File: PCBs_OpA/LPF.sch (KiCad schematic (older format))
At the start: 9 parts, among them J2 ANT

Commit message: operational amplifier Direct detection receiver
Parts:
- L10, L6, L8: footprint Choke_Axial_ThroughHole:Choke_Horizontal_RM20mm -> Choke_Toroid_ThroughHole:Choke_Toroid_6,5x13mm_Vertical
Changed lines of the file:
@@
 F 0 "L6" V 5400 2450 50  0000 L CNN
 F 1 "1.32uH" V 5300 2250 50  0000 L CNN
-F 2 "Choke_Axial_ThroughHole:Choke_Horizontal_RM20mm" H 5200 2400 50  0001 C CNN
+F 2 "Choke_Toroid_ThroughHole:Choke_Toroid_6,5x13mm_Vertical" H 5200 2400 50  0001 C CNN
 F 3 "" H 5200 2400 50  0001 C CNN
 	1    5200 2400
@@
 F 0 "L8" V 6050 2450 50  0000 L CNN
 F 1 "1.72uH" V 5950 2250 50  0000 L CNN
-F 2 "Choke_Axial_ThroughHole:Choke_Horizontal_RM20mm" H 5850 2400 50  0001 C CNN
+F 2 "Choke_Toroid_ThroughHole:Choke_Toroid_6,5x13mm_Vertical" H 5850 2400 50  0001 C CNN
 F 3 "" H 5850 2400 50  0001 C CNN
 	1    5850 2400
@@
 F 0 "L10" V 6700 2450 50  0000 L CNN
 F 1 "1.32uH" V 6600 2250 50  0000 L CNN
-F 2 "Choke_Axial_ThroughHole:Choke_Horizontal_RM20mm" H 6500 2400 50  0001 C CNN
+F 2 "Choke_Toroid_ThroughHole:Choke_Toroid_6,5x13mm_Vertical" H 6500 2400 50  0001 C CNN
 F 3 "" H 6500 2400 50  0001 C CNN
 	1    6500 2400

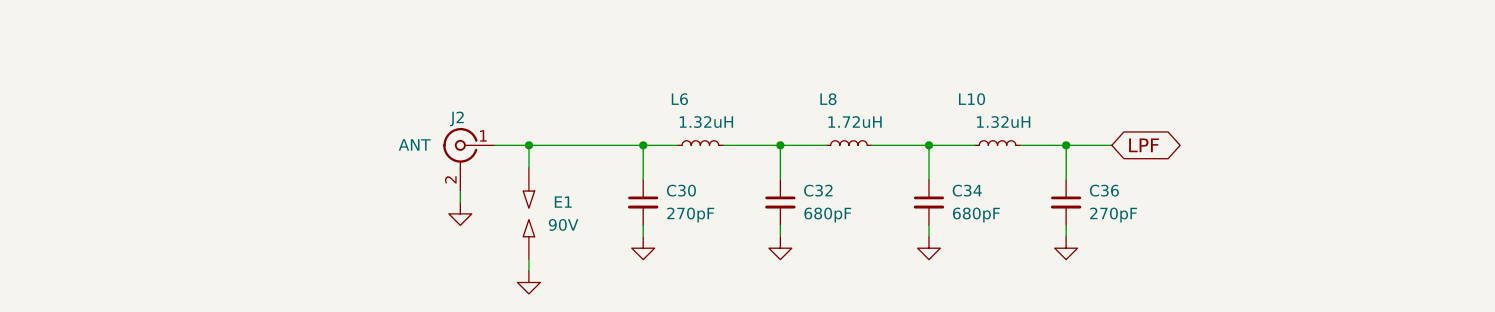
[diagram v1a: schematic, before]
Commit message: add LPF/HPF RFSimm models
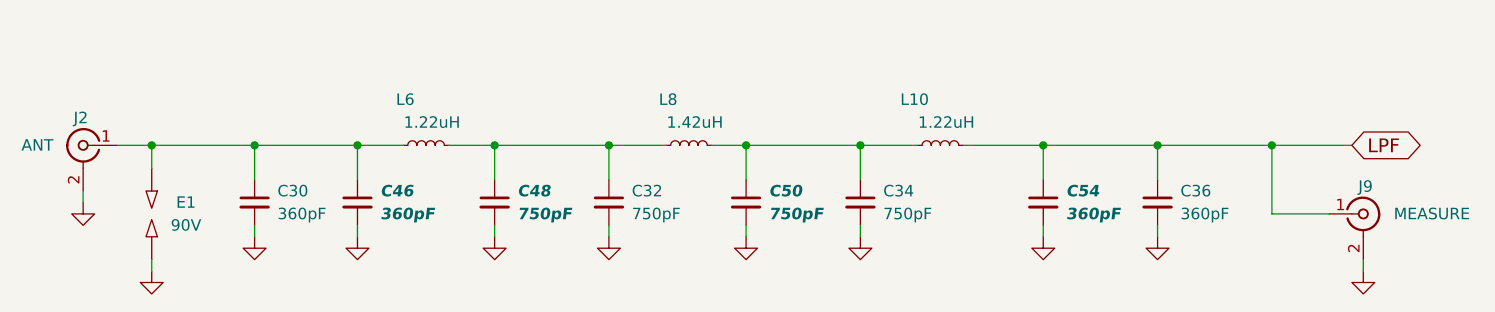
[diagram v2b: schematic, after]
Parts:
- added C46, C54: 360pF, LCSDR:C_1206_0603, symbol C_Small
- added C48, C50: 750pF, LCSDR:C_1206_0603, symbol C_Small
- added J9: MEASURE, LCSDR:U.FL_Molex_MCRF_73412-0110_Vertical, symbol Conn_Coaxial
- C30, C36: value 270pF -> 360pF
- C32, C34: value 680pF -> 750pF
- L10, L6: value 1.32uH -> 1.22uH
- L8: value 1.72uH -> 1.42uH
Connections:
- net GND: now also C46.2, C48.2, C50.2, C54.2, J9.2 (Ext)
- net LPF: now also C54.1, J9.1 (In)
- net at C30.1, E1.1, J2.1 (In)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: now also C46.1
- net at C32.1, L6.2, L8.1: now also C48.1
- net at C34.1, L10.1, L8.2: now also C50.1
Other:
- moved on the sheet: C30, C32, C34, C36, E1, J2, L10, L6, L8

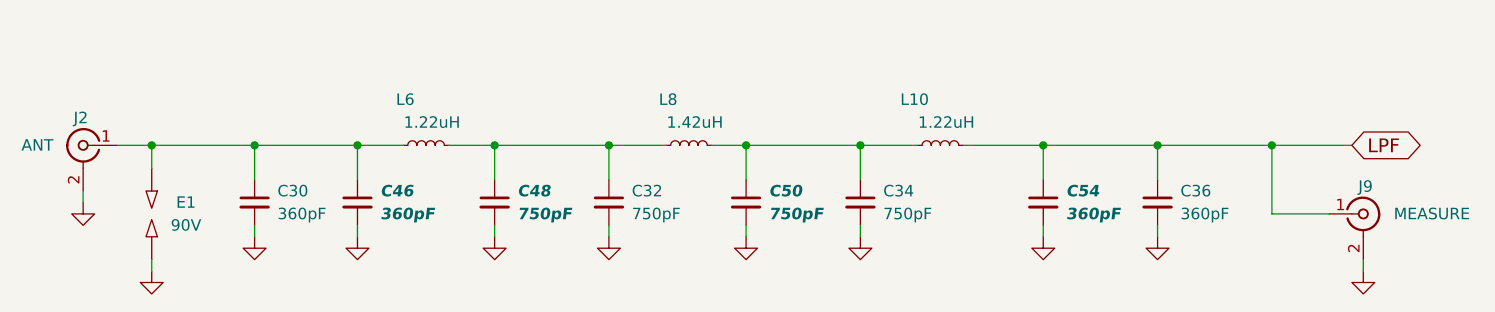
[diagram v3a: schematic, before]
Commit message: add text to HPF/LPF sch
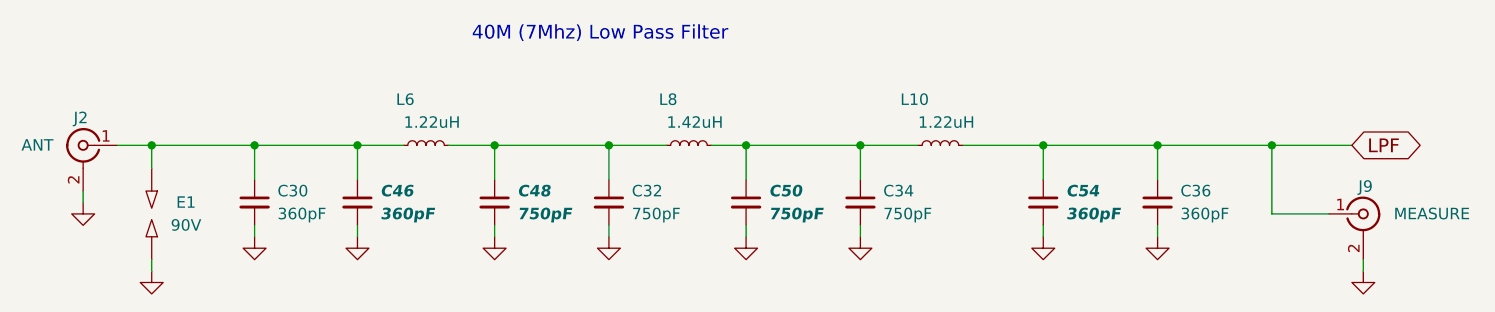
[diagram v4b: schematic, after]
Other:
- note added: "40M (7Mhz) Low Pass Filter"
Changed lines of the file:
@@
 $EndComp
 $Comp
-L GND #PWR103
+L GND #PWR0100
 U 1 1 630B845A
 P 3250 2800
-F 0 "#PWR103" H 3250 2550 50  0001 C CNN
+F 0 "#PWR0100" H 3250 2550 50  0001 C CNN
 F 1 "GND" H 3250 2650 50  0001 C CNN
 F 2 "" H 3250 2800 50  0001 C CNN
@@
 	3250 2800 3250 2750
 $Comp
-L GND #PWR105
+L GND #PWR0101
 U 1 1 630B84B3
 P 4300 2800
-F 0 "#PWR105" H 4300 2550 50  0001 C CNN
+F 0 "#PWR0101" H 4300 2550 50  0001 C CNN
 F 1 "GND" H 4300 2650 50  0001 C CNN
 F 2 "" H 4300 2800 50  0001 C CNN
@@
 	4300 2800 4300 2750
 $Comp
-L GND #PWR108
+L GND #PWR0102
 U 1 1 630B84EC
 P 5900 2800
-F 0 "#PWR108" H 5900 2550 50  0001 C CNN
+F 0 "#PWR0102" H 5900 2550 50  0001 C CNN
 F 1 "GND" H 5900 2650 50  0001 C CNN
 F 2 "" H 5900 2800 50  0001 C CNN
@@
 	7200 2400 7200 2550
 $Comp
-L GND #PWR110
+L GND #PWR0103
 U 1 1 630B859B
 P 7200 2800
-F 0 "#PWR110" H 7200 2550 50  0001 C CNN
+F 0 "#PWR0103" H 7200 2550 50  0001 C CNN
 F 1 "GND" H 7200 2650 50  0001 C CNN
 F 2 "" H 7200 2800 50  0001 C CNN
@@
 Connection ~ 2800 2400
 $Comp
-L GND #PWR102
+L GND #PWR0104
 U 1 1 630B8EE3
 P 2800 2950
-F 0 "#PWR102" H 2800 2700 50  0001 C CNN
+F 0 "#PWR0104" H 2800 2700 50  0001 C CNN
 F 1 "GND" H 2800 2800 50  0001 C CNN
 F 2 "" H 2800 2950 50  0001 C CNN
@@
 	2800 2950 2800 2900
 $Comp
-L GND #PWR101
+L GND #PWR0105
 U 1 1 630B8F7F
 P 2500 2650
-F 0 "#PWR101" H 2500 2400 50  0001 C CNN
+F 0 "#PWR0105" H 2500 2400 50  0001 C CNN
 F 1 "GND" H 2500 2500 50  0001 C CNN
 F 2 "" H 2500 2650 50  0001 C CNN
@@
 $EndComp
 $Comp
-L GND #PWR111
+L GND #PWR0106
 U 1 1 6313C89E
 P 8100 2950
-F 0 "#PWR111" H 8100 2700 50  0001 C CNN
+F 0 "#PWR0106" H 8100 2700 50  0001 C CNN
 F 1 "GND" H 8100 2800 50  0001 C CNN
 F 2 "" H 8100 2950 50  0001 C CNN
@@
 $EndComp
 $Comp
-L GND #PWR104
+L GND #PWR0107
 U 1 1 631ABCA0
 P 3700 2800
-F 0 "#PWR104" H 3700 2550 50  0001 C CNN
+F 0 "#PWR0107" H 3700 2550 50  0001 C CNN
 F 1 "GND" H 3700 2650 50  0001 C CNN
 F 2 "" H 3700 2800 50  0001 C CNN
@@
 $EndComp
 $Comp
-L GND #PWR106
+L GND #PWR0108
 U 1 1 631ABEC6
 P 4800 2800
-F 0 "#PWR106" H 4800 2550 50  0001 C CNN
+F 0 "#PWR0108" H 4800 2550 50  0001 C CNN
 F 1 "GND" H 4800 2650 50  0001 C CNN
 F 2 "" H 4800 2800 50  0001 C CNN
@@
 Connection ~ 5400 2400
 $Comp
-L GND #PWR107
+L GND #PWR0109
 U 1 1 631AC22D
 P 5400 2800
-F 0 "#PWR107" H 5400 2550 50  0001 C CNN
+F 0 "#PWR0109" H 5400 2550 50  0001 C CNN
 F 1 "GND" H 5400 2650 50  0001 C CNN
 F 2 "" H 5400 2800 50  0001 C CNN
@@
 $EndComp
 $Comp
-L GND #PWR109
+L GND #PWR0110
 U 1 1 631AC42C
 P 6700 2800
-F 0 "#PWR109" H 6700 2550 50  0001 C CNN
+F 0 "#PWR0110" H 6700 2550 50  0001 C CNN
 F 1 "GND" H 6700 2650 50  0001 C CNN
 F 2 "" H 6700 2800 50  0001 C CNN
@@
 	6700 2400 6700 2550
 Connection ~ 6700 2400
+Text Notes 4200 1950 0    60   ~ 0
+40M (7Mhz) Low Pass Filter
 $EndSCHEMATC
